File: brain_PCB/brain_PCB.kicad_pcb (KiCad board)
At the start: 4 copper layers, 95.5 x 91 mm, 73 parts, among them J1 Conn_01x02, J10 Conn_01x02, J11 USB-C PROGRAM, J2 Conn_01x02, J3 Conn_01x02, J4 Conn_01x03, J5 Conn_01x03, J6 Conn_01x04, J7 Conn_01x14, J8 Conn_01x06, J9 Conn_01x08, SW1 SW_Push, SW2 BOOT, U1 STM32H753ZITx, U2 USBLC6-2SC6, Y1 8 MHz, Y2 32.768 kHz

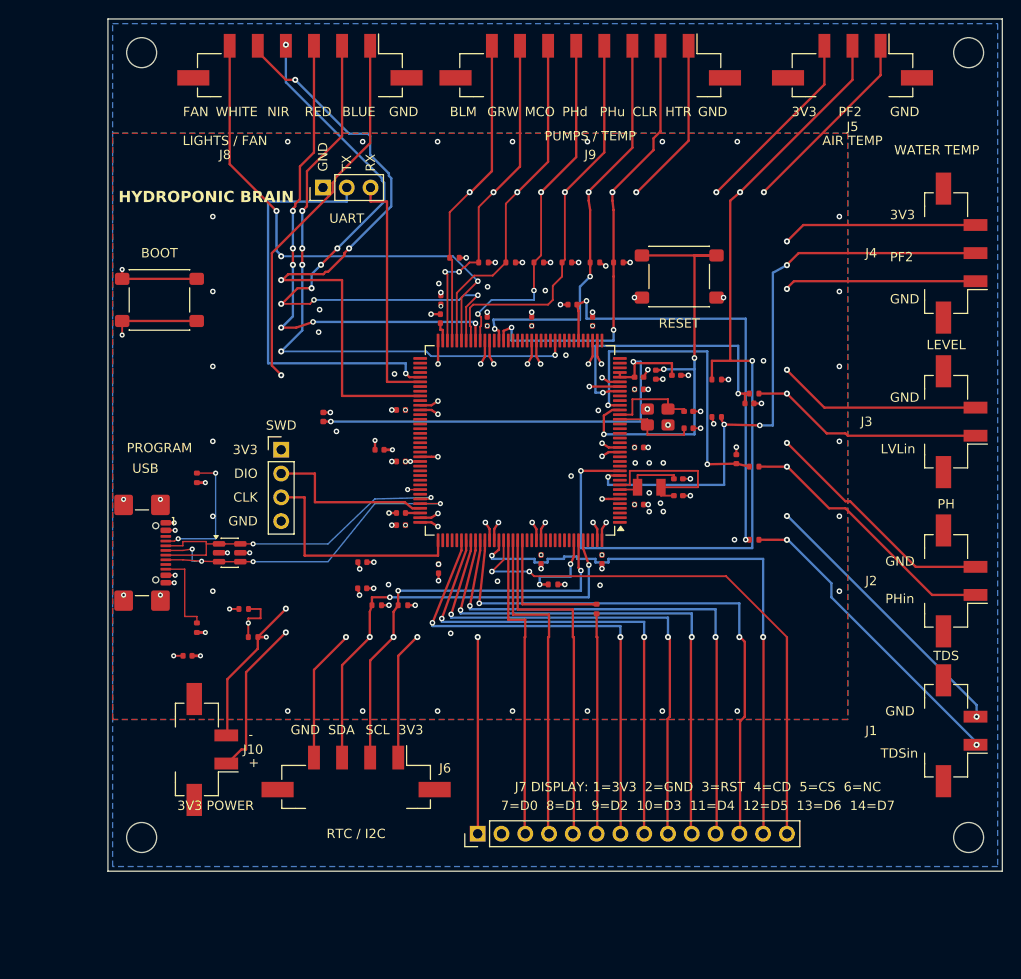
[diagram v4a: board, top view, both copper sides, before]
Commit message: Update four KiCad designs and include portable project libraries
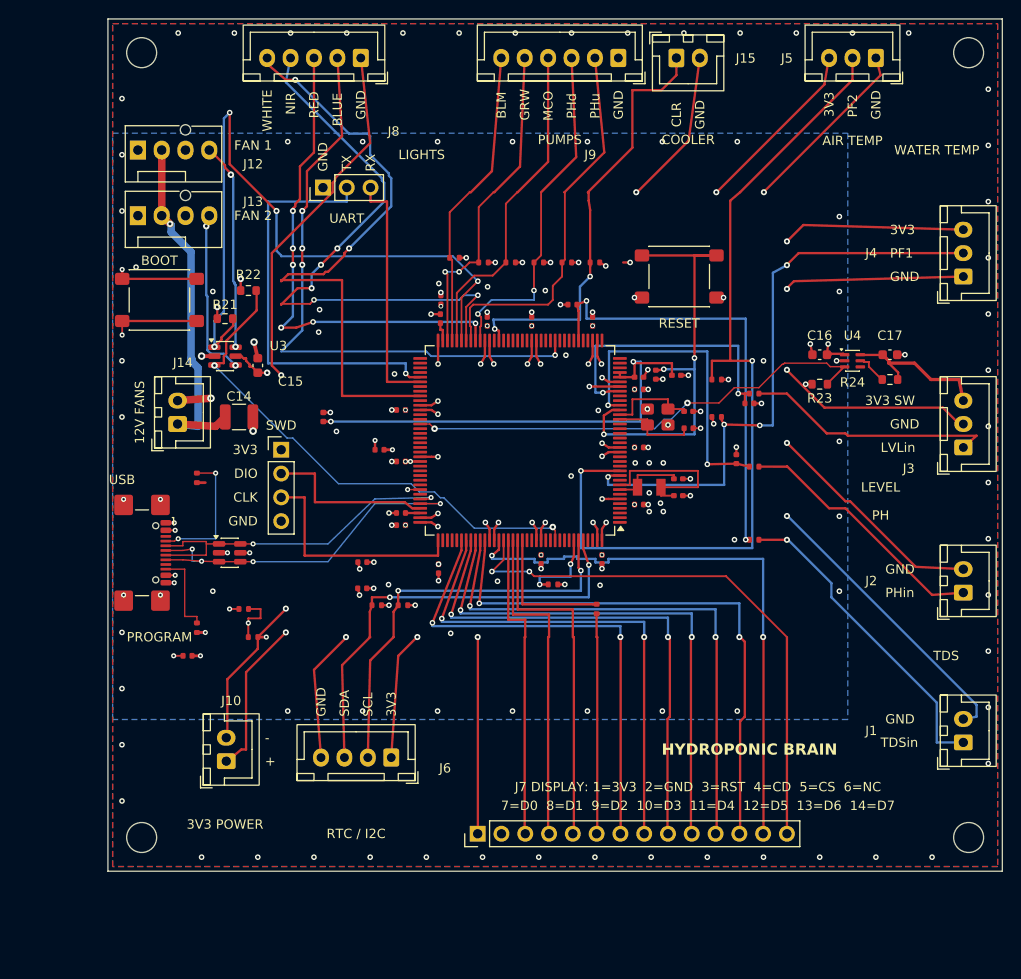
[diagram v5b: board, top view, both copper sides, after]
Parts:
- removed R10: 10k, Resistor_SMD:R_0402_1005Metric
- added C14: 10uF 50V X7R, Capacitor_SMD:C_1210_3225Metric, F.Cu at (36.5, 54.5)
- added C15: 100nF 50V X7R, Capacitor_SMD:C_0603_1608Metric, F.Cu at (38.5, 49.0)
- added C16: 1uF 16V X7R, Capacitor_SMD:C_0603_1608Metric, F.Cu at (98.5, 47.9)
- added C17: 100nF 50V X7R, Capacitor_SMD:C_0603_1608Metric, F.Cu at (106.0, 47.9)
- added J12: FAN 1 - P12 PRO, Connector:FanPinHeader_1x04_P2.54mm_Vertical, F.Cu at (25.7, 26.0)
- added J13: FAN 2 - P12 PRO, Connector:FanPinHeader_1x04_P2.54mm_Vertical, F.Cu at (25.7, 33.0)
- added J14: 12V FAN POWER, Connector_JST:JST_XH_B2B-XH-A_1x02_P2.50mm_Vertical, F.Cu at (29.9, 55.2)
- added J15: COOLER, Connector_JST:JST_XH_B2B-XH-A_1x02_P2.50mm_Vertical, F.Cu at (83.2, 16.2)
- added R21: 10k, Resistor_SMD:R_0603_1608Metric, F.Cu at (35.0, 44.0)
- added R22: 10k, Resistor_SMD:R_0603_1608Metric, F.Cu at (37.5, 41.0)
- added R23: 100k, Resistor_SMD:R_0603_1608Metric, F.Cu at (98.5, 51.0)
- added R24: 100, Resistor_SMD:R_0603_1608Metric, F.Cu at (106.0, 50.5)
- added U3: SN74LVC2G07DBVR, Package_TO_SOT_SMD:SOT-23-6, F.Cu at (35.0, 48.0)
- added U4: TPS22919DCKR, Package_TO_SOT_SMD:SOT-363_SC-70-6, F.Cu at (102.0, 48.5)
- C1, decoupl_C1, decoupl_C2, decoupl_C3, rescaps_C1, rescaps_C2: footprint Capacitor_SMD:C_0402_1005Metric -> BrainReviewed:C_0402_1005Metric_Reviewed_7
- C10, C11, C5, C9: footprint Capacitor_SMD:C_0402_1005Metric -> BrainReviewed:C_0402_1005Metric_Reviewed_4
- C12, C13: footprint Capacitor_SMD:C_0402_1005Metric -> BrainReviewed:C_0402_1005Metric_Reviewed_3
- C2: footprint Capacitor_SMD:C_0402_1005Metric -> BrainReviewed:C_0402_1005Metric_Reviewed_2
- C3: footprint Capacitor_SMD:C_0402_1005Metric -> BrainReviewed:C_0402_1005Metric_Reviewed_10
- C4: footprint Capacitor_SMD:C_0402_1005Metric -> BrainReviewed:C_0402_1005Metric_Reviewed_8
- C6: footprint Capacitor_SMD:C_0402_1005Metric -> BrainReviewed:C_0402_1005Metric_Reviewed_9
- C7, decoupl_C4, decoupl_C5, decoupl_C7: footprint Capacitor_SMD:C_0402_1005Metric -> BrainReviewed:C_0402_1005Metric_Reviewed_6
- C8: footprint Capacitor_SMD:C_0402_1005Metric -> BrainReviewed:C_0402_1005Metric_Reviewed_12
- J1, J10, J2: footprint Connector_Molex:Molex_Micro-Fit_3.0_43650-0224_1x02-1MP_P3.00mm_Vertical -> Connector_JST:JST_XH_B2B-XH-A_1x02_P2.50mm_Vertical
- J3: value Conn_01x02 -> LEVEL SENSOR - ADAFRUIT 4965; footprint Connector_Molex:Molex_Micro-Fit_3.0_43650-0224_1x02-1MP_P3.00mm_Vertical -> Connector_JST:JST_XH_B3B-XH-A_1x03_P2.50mm_Vertical
- J4, J5: footprint Connector_Molex:Molex_Micro-Fit_3.0_43650-0324_1x03-1MP_P3.00mm_Vertical -> Connector_JST:JST_XH_B3B-XH-A_1x03_P2.50mm_Vertical
- J6: footprint Connector_Molex:Molex_Micro-Fit_3.0_43650-0424_1x04-1MP_P3.00mm_Vertical -> Connector_JST:JST_XH_B4B-XH-A_1x04_P2.50mm_Vertical
- J8: value Conn_01x06 -> LIGHT BOARD; footprint Connector_Molex:Molex_Micro-Fit_3.0_43650-0624_1x06-1MP_P3.00mm_Vertical -> Connector_JST:JST_XH_B5B-XH-A_1x05_P2.50mm_Vertical
- J9: value Conn_01x08 -> PUMP BOARD; footprint Connector_Molex:Molex_Micro-Fit_3.0_43650-0824_1x08-1MP_P3.00mm_Vertical -> Connector_JST:JST_XH_B6B-XH-A_1x06_P2.50mm_Vertical
- R1, R2, R3: footprint Resistor_SMD:R_0402_1005Metric -> BrainReviewed:R_0402_1005Metric_Reviewed_2
- R11, R12, R13, R14, R15, R16, R4, R5: footprint Resistor_SMD:R_0402_1005Metric -> BrainReviewed:R_0402_1005Metric_Reviewed_1
- R17, R18: footprint Resistor_SMD:R_0402_1005Metric -> BrainReviewed:R_0402_1005Metric_Reviewed_5
- R19, R6: footprint Resistor_SMD:R_0402_1005Metric -> BrainReviewed:R_0402_1005Metric_Reviewed_6
- R20: footprint Resistor_SMD:R_0402_1005Metric -> BrainReviewed:R_0402_1005Metric_Reviewed_4
- R7, R8: value 1.9k -> 1.91k; footprint Resistor_SMD:R_0402_1005Metric -> BrainReviewed:R_0402_1005Metric_Reviewed_2
- R9: footprint Resistor_SMD:R_0402_1005Metric -> BrainReviewed:R_0402_1005Metric_Reviewed_3
- VCAP_C1, decoupl_C10, decoupl_C8, decoupl_C9: footprint Capacitor_SMD:C_0402_1005Metric -> BrainReviewed:C_0402_1005Metric_Reviewed_1
- Y1: footprint Crystal:Crystal_SMD_3225-4Pin_3.2x2.5mm -> BrainReviewed:Crystal_SMD_3225-4Pin_3.2x2.5mm_Reviewed_1
- Y2: footprint Crystal:Crystal_SMD_3215-2Pin_3.2x1.5mm -> BrainReviewed:Crystal_SMD_3215-2Pin_3.2x1.5mm_Reviewed_1
- decoupl_C11, decoupl_C12: footprint Capacitor_SMD:C_0402_1005Metric -> BrainReviewed:C_0402_1005Metric_Reviewed_13
- decoupl_C13: footprint Capacitor_SMD:C_0402_1005Metric -> BrainReviewed:C_0402_1005Metric_Reviewed_5
- decoupl_C6: footprint Capacitor_SMD:C_0402_1005Metric -> BrainReviewed:C_0402_1005Metric_Reviewed_11
- moved J8 6.75 mm to (49.5, 16.2)
- moved J6 4.89 mm to (52.8, 90.9)
- moved J9 3.52 mm to (77.0, 16.2)
- moved J10 3.38 mm to (35.1, 91.2)
- moved J3 3.31 mm to (113.8, 57.8)
- moved J5 3.10 mm to (104.5, 16.2)
- moved J4 3.10 mm to (113.8, 39.5)
- moved J1 2.22 mm to (113.8, 89.2)
- moved J2 2.22 mm to (113.8, 73.2)
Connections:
- J9 pad 2: /HEATER -> /PH_UP
- J9 pad 3: /COOLER -> /PH_DOWN
- J9 pad 4: /PH_UP -> /FLORA_MICRO
- J9 pad 5: /PH_DOWN -> /FLORA_GROW
- J9 pad 6: /FLORA_MICRO -> /FLORA_BLOOM
- U1 pad 134: unconnected-(U1-PB4-Pad134) -> /FAN2_PWM
- U1 pad 58: /HEATER -> unconnected-(U1-PE7-Pad58)
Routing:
- net /FAN2_PWM: track 0.00 -> 55.3 mm, vias 0 -> 2
- net /LEVEL_PWR: track 0.00 -> 51.3 mm, vias 0 -> 2
- net /HEATER: track 48.3 -> 0.00 mm, vias 3 -> 0
- net /FAN_12V: track 0.00 -> 38.9 mm, vias 0 -> 1
- net /FAN_PWM: track 54.1 -> 76.4 mm, vias 3 -> 4
- net /FAN1_CTL: track 0.00 -> 22.2 mm, vias 0 -> 2
- net /FAN2_CTL: track 0.00 -> 18.4 mm, vias 0 -> 2
- net /LEVEL_3V3: track 0.00 -> 17.5 mm
- net +3V3: track 141.9 -> 149.3 mm, vias 44 -> 48
- net GND: track 264.1 -> 270.3 mm, vias 116 -> 169
- net /LEVEL_DISCHG: track 0.00 -> 3.46 mm
- net /COOLER: track 44.2 -> 46.4 mm, vias 3 -> 2
- net /LEVEL_IN: track 25.2 -> 27.0 mm, vias 1 -> 0
- net /WHITE_PWM: track 67.6 -> 65.9 mm, vias 3 -> 2
- net /FLORA_MICRO: track 36.9 -> 35.4 mm, vias 1 -> 0
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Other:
- board text added: "12V FANS"
- board text added: "3V3 SW"
- board text added: "COOLER"
- board text added: "FAN 1"
- board text added: "FAN 2"
- board text added: "LIGHTS"
- board text added: "PF1"
- board text added: "PUMPS"
- board text removed: "FAN"
- board text removed: "HTR"
- board text removed: "LIGHTS / FAN"
- board text removed: "PUMPS / TEMP"
